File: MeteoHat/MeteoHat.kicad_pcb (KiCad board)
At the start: 2 copper layers, 63 x 61 mm, 6 parts, among them J1 RaspberryPI, SW1 SW_Push, U1 BME680, U2 BH1750

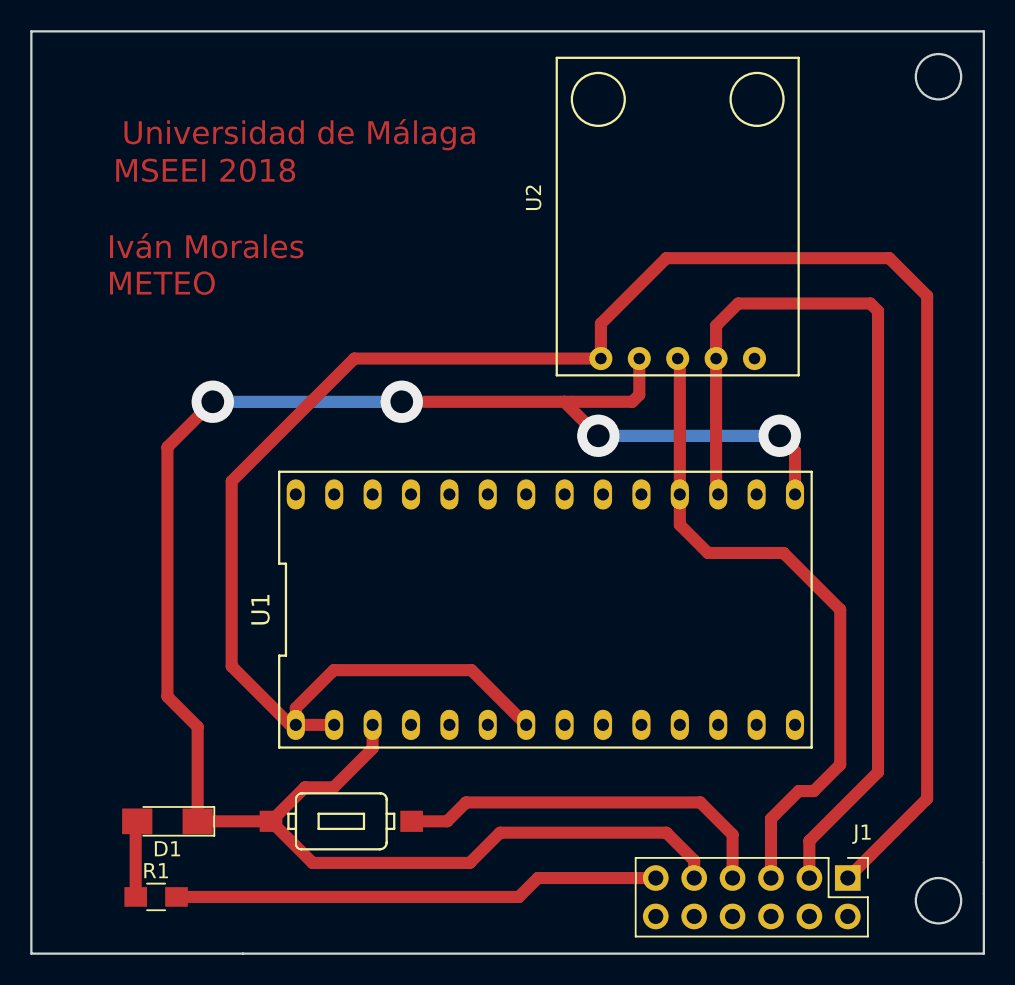
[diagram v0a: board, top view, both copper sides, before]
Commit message: Added PCB Keepout Zones
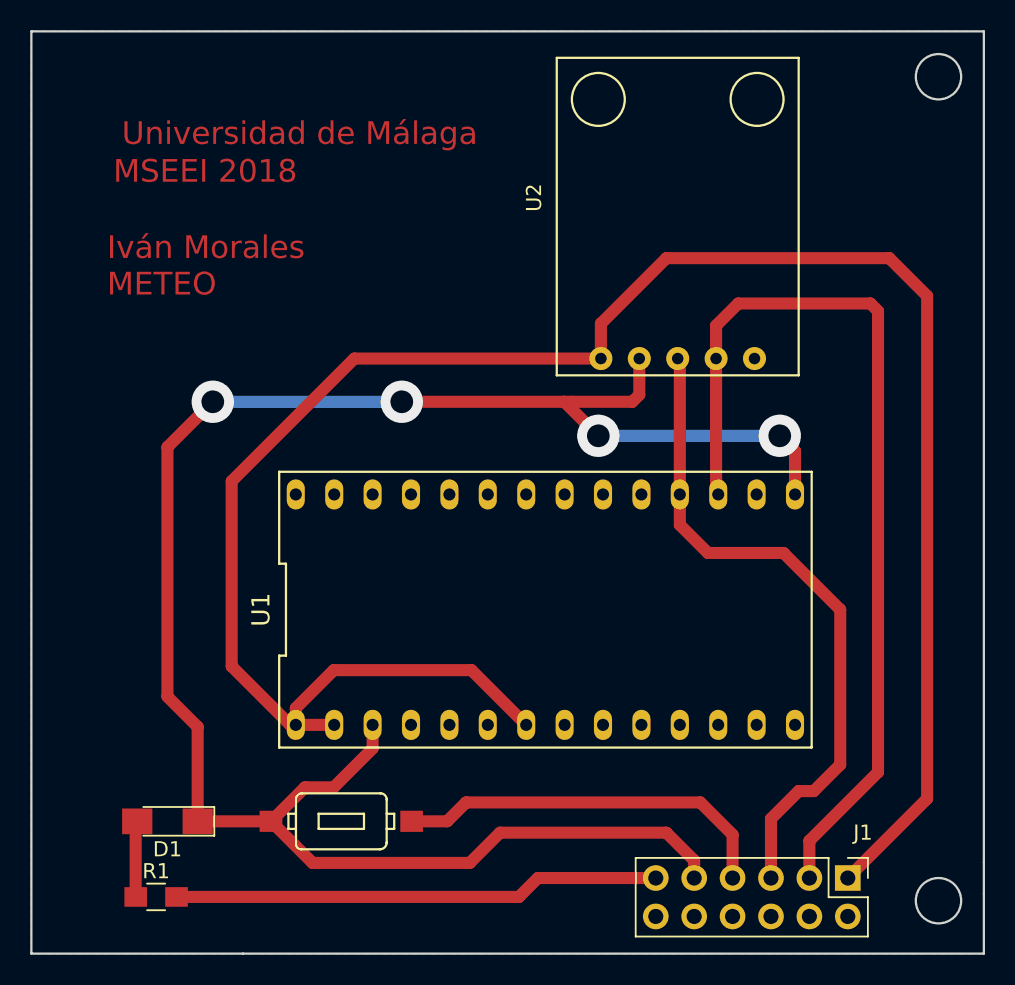
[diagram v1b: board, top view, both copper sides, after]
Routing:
- added copper zone on F.Cu, net GND
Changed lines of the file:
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@@
     (last_trace_width 0.8)
     (trace_clearance 0.2)
-    (zone_clearance 0.508)
+    (zone_clearance 1.508)
     (zone_45_only no)
     (trace_min 0.2)
@@
   (segment (start 61.5 80) (end 69.3 80) (width 0.8) (layer F.Cu) (net 34))
   (segment (start 60.25 81.25) (end 61.5 80) (width 0.8) (layer F.Cu) (net 34))
+  (zone (net 4) (net_name GND) (layer F.Cu) (hatch edge 0.508)
+    (connect_pads (clearance 1.508))
+    (min_thickness 0.508)
+    (fill yes (arc_segments 16) (thermal_gap 0.8) (thermal_bridge_width 0.8))
+    (polygon
+      (pts
+        (xy 91 85) (xy 28 85) (xy 28 24) (xy 91 24)
+      )
+    )
+  )
 )
